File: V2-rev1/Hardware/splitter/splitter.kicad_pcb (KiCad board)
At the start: 2 copper layers, 29 parts, among them J0 Rpi_40Pin_F, J1 Control_seg:1, J2 Control_seg:2, J3 Control_seg:3, J4 Molex_PSU_F, J5 USB_A_F, J6 Siren, J7 Siren, K0 RELRAS0515, Q1 BD139-16

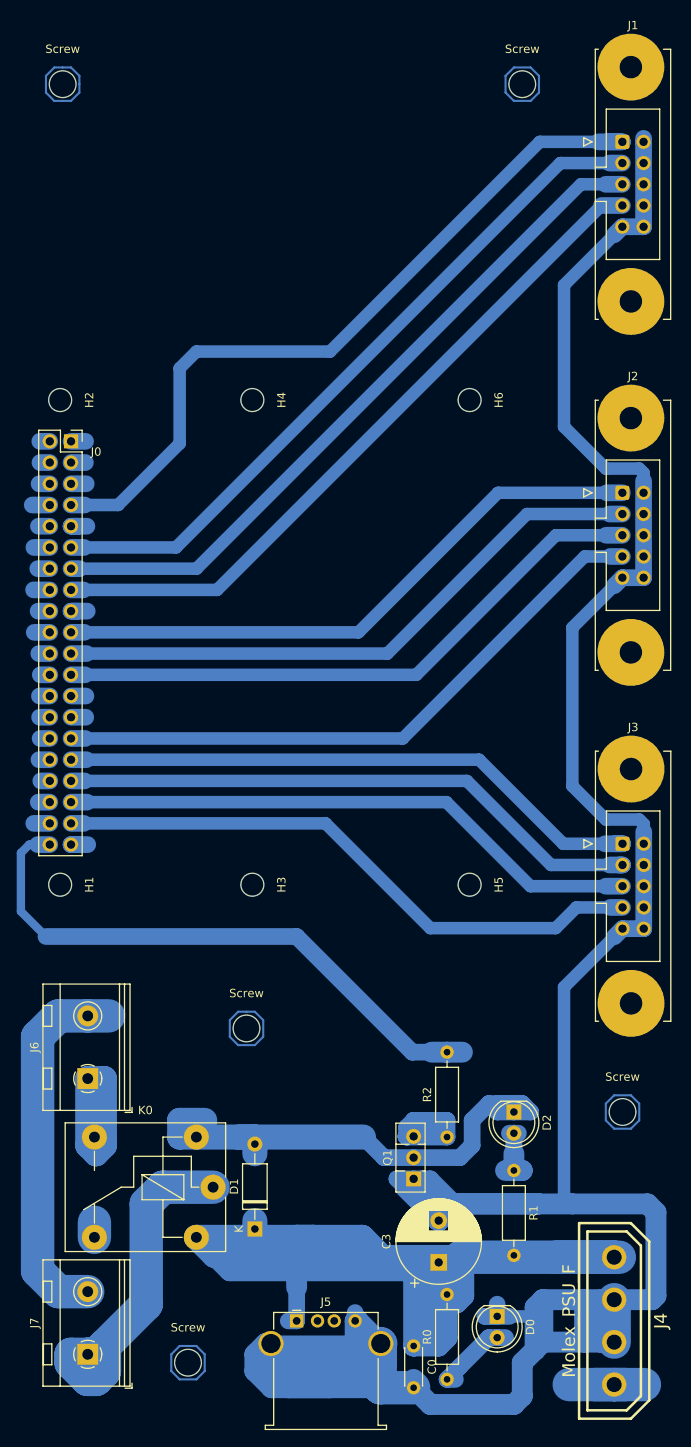
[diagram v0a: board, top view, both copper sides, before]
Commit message: make way for usb
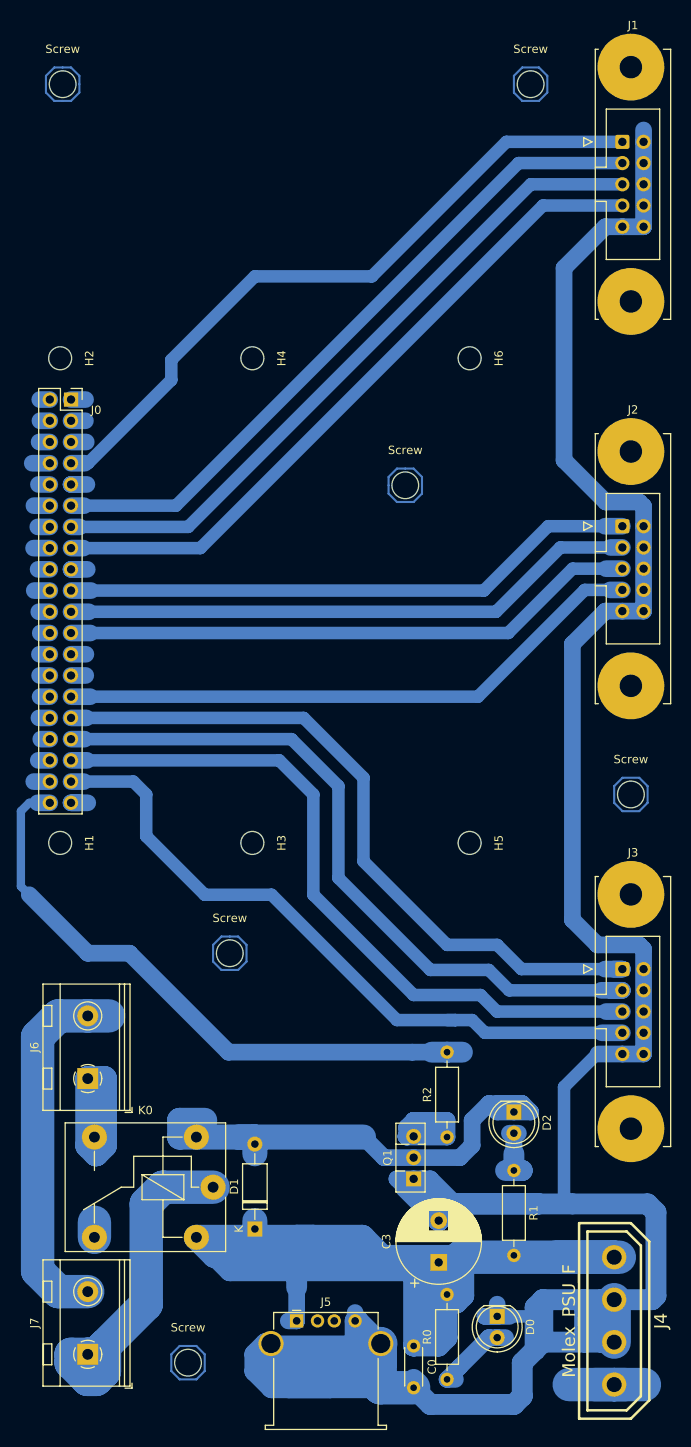
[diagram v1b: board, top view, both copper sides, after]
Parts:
- removed the Screw at (77.0, 145.0)
- removed the Screw at (122.0, 155.0)
- removed the Screw at (110.0, 32.0)
- added Screw: MountingHole_3.2mm_M3, MountingHole:MountingHole_3.2mm_M3, F.Cu at (96.0, 80.0)
- added Screw: MountingHole_3.2mm_M3, MountingHole:MountingHole_3.2mm_M3, F.Cu at (123.0, 117.0)
- added Screw: MountingHole_3.2mm_M3, MountingHole:MountingHole_3.2mm_M3, F.Cu at (75.0, 136.0)
- added Screw: MountingHole_3.2mm_M3, MountingHole:MountingHole_3.2mm_M3, F.Cu at (111.0, 32.0)
- moved J3 15.0 mm to (122.0, 137.9)
- moved H1 5.00 mm to (54.7, 122.8)
- moved H2 5.00 mm to (54.7, 64.8)
- moved H3 5.00 mm to (77.7, 122.8)
- moved H4 5.00 mm to (77.7, 64.8)
- moved H5 5.00 mm to (103.7, 122.8)
- moved H6 5.00 mm to (103.7, 64.8)
- moved J0 5.00 mm to (56.0, 69.7)
- moved J2 4.00 mm to (122.0, 84.9)
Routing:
- net /seg:3_bit:b_gpio:13: track 71.7 -> 87.4 mm
- net /seg:3_bit:c_gpio:19: track 70.2 -> 85.5 mm
- net /seg:3_bit:a_gpio:06: track 72.3 -> 86.4 mm
- net (no net): track 68.3 -> 81.9 mm, vias 11 -> 12
- net /seg:3_bit:d_gpio:26: track 72.2 -> 82.4 mm
- net /seg:1_bit:a_gpio:04: track 93.3 -> 84.5 mm
- net Earth: track 443.5 -> 438.6 mm
- net /seg:2_bit:a_gpio:10: track 72.9 -> 69.2 mm
- net /seg:2_bit:d_gpio:05: track 75.0 -> 71.3 mm
- net /seg:2_bit:c_gpio:11: track 72.9 -> 69.2 mm
- net /seg:2_bit:b_gpio:09: track 72.9 -> 69.3 mm
- net /SIREN_gpio:21: track 70.7 -> 73.9 mm
- net /seg:1_bit:d_gpio:22: track 85.0 -> 83.0 mm
- net /seg:1_bit:c_gpio:27: track 85.0 -> 83.0 mm
- net /seg:1_bit:b_gpio:17: track 85.0 -> 83.0 mm

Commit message: mark pin 1
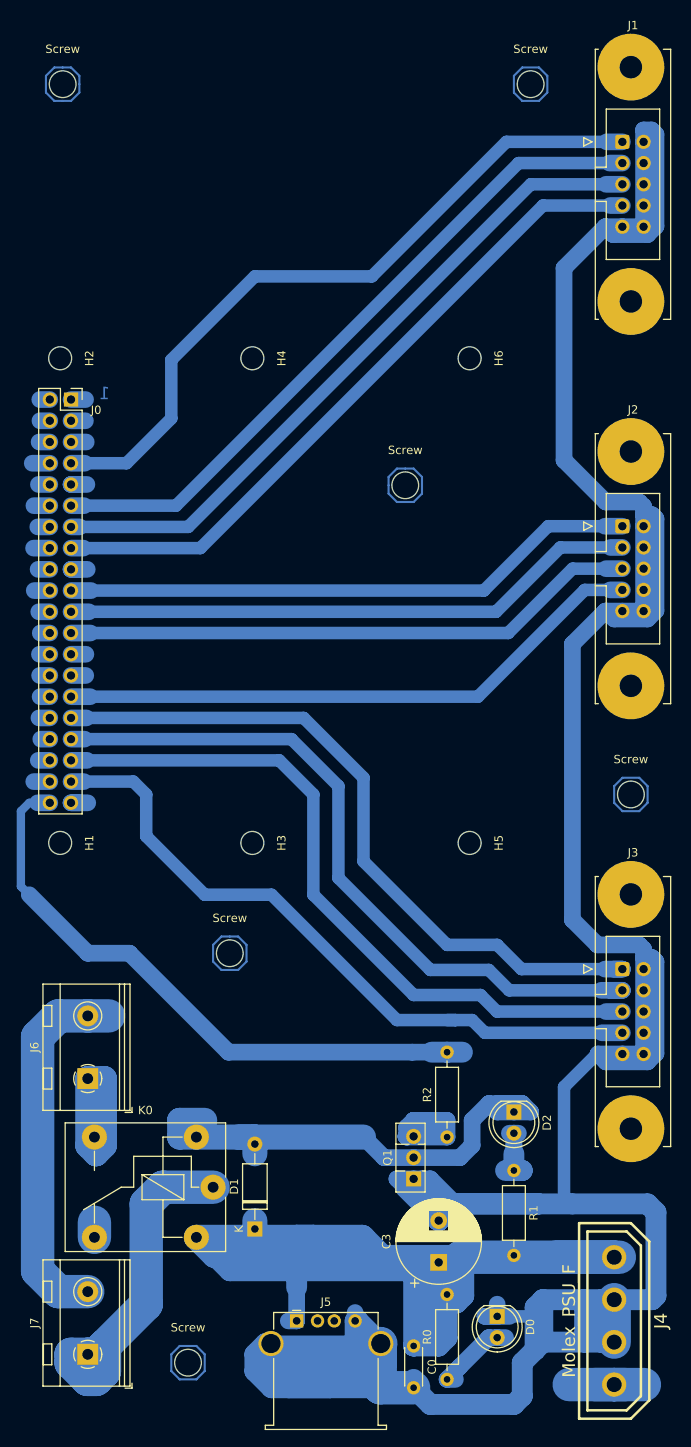
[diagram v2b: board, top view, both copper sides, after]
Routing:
- net Earth: track 438.6 -> 498.0 mm
- net /seg:1_bit:a_gpio:04: track 84.5 -> 87.6 mm
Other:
- board text added: "1"
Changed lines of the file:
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@@
   (general
     (thickness 1.6)
-    (drawings 16)
-    (tracks 461)
+    (drawings 17)
+    (tracks 487)
     (zones 0)
     (modules 30)
@@
   )
   (setup
-    (last_trace_width 1.5)
+    (last_trace_width 2)
     (user_trace_width 1)
     (user_trace_width 1.5)
@@
       (effects (font (size 1 1) (thickness 0.15)))
     )
-    (fp_text user %R (at 0.3 0) (layer F.Fab)
-      (effects (font (size 1 1) (thickness 0.15)))
-    )
     (fp_circle (center 0 0) (end 3.45 0) (layer F.CrtYd) (width 0.05))
     (fp_circle (center 0 0) (end 3.2 0) (layer Cmts.User) (width 0.15))
+    (fp_text user %R (at 0.3 0) (layer F.Fab)
+      (effects (font (size 1 1) (thickness 0.15)))
+    )
     (pad 1 np_thru_hole circle (at 0 0) (size 3.2 3.2) (drill 3.2) (layers *.Cu *.Mask))
   )
@@
       (effects (font (size 1 1) (thickness 0.15)))
     )
-    (fp_text user %R (at 0.3 0) (layer F.Fab)
-      (effects (font (size 1 1) (thickness 0.15)))
-    )
     (fp_circle (center 0 0) (end 3.45 0) (layer F.CrtYd) (width 0.05))
     (fp_circle (center 0 0) (end 3.2 0) (layer Cmts.User) (width 0.15))
+    (fp_text user %R (at 0.3 0) (layer F.Fab)
+      (effects (font (size 1 1) (thickness 0.15)))
+    )
     (pad 1 np_thru_hole circle (at 0 0) (size 3.2 3.2) (drill 3.2) (layers *.Cu *.Mask))
   )
@@
     )
     (fp_text value Control_seg:2 (at 1.27 24.1) (layer F.Fab)
-      (effects (font (size 1 1) (thickness 0.15)))
-    )
-    (fp_text user %R (at 1.27 5.08 90) (layer F.Fab)
       (effects (font (size 1 1) (thickness 0.15)))
     )
@@
     (fp_line (start -2.13 -10.97) (end 5.67 -10.97) (layer F.Fab) (width 0.1))
     (fp_line (start -3.13 -9.97) (end -2.13 -10.97) (layer F.Fab) (width 0.1))
+    (fp_text user %R (at 1.27 5.08 90) (layer F.Fab)
+      (effects (font (size 1 1) (thickness 0.15)))
+    )
     (pad 1 thru_hole roundrect (at 0 0) (size 1.7 1.7) (drill 1) (layers *.Cu *.Mask) (roundrect_rratio 0.1470588235294118)
       (net 24 /seg:2_bit:a_gpio:10))
@@
     )
   )
+  (gr_text 1 (at 60 69) (layer B.Cu)
+    (effects (font (size 1.5 1.5) (thickness 0.3)) (justify mirror))
+  )
   (gr_line (start 107.2 123.3) (end 107.2 64.3) (layer Eco2.User) (width 0.2))
   (gr_arc (start 104.2 123.3) (end 104.2 126.3) (angle -90) (layer Eco2.User) (width 0.2))
@@
   (segment (start 115 165) (end 115 152) (width 1.5) (layer B.Cu) (net 1))
   (segment (start 116 166) (end 115 165) (width 1.5) (layer B.Cu) (net 1))
-  (segment (start 124.52 137.9) (end 124.52 135.52) (width 1.5) (layer B.Cu) (net 1))
   (segment (start 124.52 148.06) (end 124.52 135.52) (width 2) (layer B.Cu) (net 1))
   (segment (start 124.52 148.06) (end 124.52 137.9) (width 1.5) (layer B.Cu) (net 1))
@@
   (segment (start 124.52 95.06) (end 124.52 84.9) (width 2) (layer B.Cu) (net 1))
   (segment (start 116 132) (end 116 99) (width 2) (layer B.Cu) (net 1))
-  (segment (start 119.94 95.06) (end 121.98 95.06) (width 2) (layer B.Cu) (net 1))
   (segment (start 116 99) (end 119.94 95.06) (width 2) (layer B.Cu) (net 1))
   (segment (start 124 135) (end 124.52 135.52) (width 2) (layer B.Cu) (net 1))
@@
   (segment (start 124.52 82.52) (end 124 82) (width 2) (layer B.Cu) (net 1))
   (segment (start 124 82) (end 120 82) (width 2) (layer B.Cu) (net 1))
-  (segment (start 124.52 84.9) (end 124.52 82.52) (width 2) (layer B.Cu) (net 1))
+  (segment (start 124.52 37.48) (end 125.48 37.48) (width 2) (layer B.Cu) (net 1))
+  (segment (start 125.48 37.48) (end 126 38) (width 2) (layer B.Cu) (net 1))
+  (segment (start 126 38) (end 126 49) (width 2) (layer B.Cu) (net 1))
+  (segment (start 126 49) (end 125 50) (width 2) (layer B.Cu) (net 1))
+  (segment (start 120.88 50) (end 119.94 49.06) (width 2) (layer B.Cu) (net 1))
+  (segment (start 125 50) (end 120.88 50) (width 2) (layer B.Cu) (net 1))
+  (segment (start 124.52 83.52) (end 125.52 83.52) (width 2) (layer B.Cu) (net 1))
+  (segment (start 124.52 84.9) (end 124.52 83.52) (width 2) (layer B.Cu) (net 1))
+  (segment (start 124.52 83.52) (end 124.52 82.52) (width 2) (layer B.Cu) (net 1))
+  (segment (start 125.52 83.52) (end 126 84) (width 2) (layer B.Cu) (net 1))
+  (segment (start 126 84) (end 126 95) (width 2) (layer B.Cu) (net 1))
+  (segment (start 126 95) (end 125 96) (width 2) (layer B.Cu) (net 1))
+  (segment (start 121 96) (end 120.06 95.06) (width 2) (layer B.Cu) (net 1))
+  (segment (start 125 96) (end 121 96) (width 2) (layer B.Cu) (net 1))
+  (segment (start 120.06 95.06) (end 121.98 95.06) (width 2) (layer B.Cu) (net 1))
+  (segment (start 119.94 95.06) (end 120.06 95.06) (width 2) (layer B.Cu) (net 1))
+  (segment (start 124.52 136.52) (end 125.52 136.52) (width 2) (layer B.Cu) (net 1))
+  (segment (start 124.52 137.9) (end 124.52 136.52) (width 1.5) (layer B.Cu) (net 1))
+  (segment (start 124.52 136.52) (end 124.52 135.52) (width 1.5) (layer B.Cu) (net 1))
+  (segment (start 125.52 136.52) (end 126 137) (width 2) (layer B.Cu) (net 1))
+  (segment (start 126 137) (end 126 148) (width 2) (layer B.Cu) (net 1))
+  (segment (start 126 148) (end 125 149) (width 2) (layer B.Cu) (net 1))
+  (segment (start 120 149) (end 119.06 148.06) (width 2) (layer B.Cu) (net 1))
+  (segment (start 125 149) (end 120 149) (width 2) (layer B.Cu) (net 1))
   (segment (start 101 187) (end 102 187) (width 2) (layer B.Cu) (net 2))
   (segment (start 102.5 185.5) (end 101 187) (width 2) (layer B.Cu) (net 2))
@@
   (segment (start 56 77.36) (end 57.202081 77.36) (width 1.5) (layer B.Cu) (net 12))
   (segment (start 56 77.36) (end 57.64 77.36) (width 2) (layer B.Cu) (net 12))
-  (segment (start 58.03773 77.36) (end 68 67.39773) (width 1.5) (layer B.Cu) (net 12))
   (segment (start 57.64 77.36) (end 58.03773 77.36) (width 1.5) (layer B.Cu) (net 12))
-  (segment (start 68 67.39773) (end 68 65) (width 1.5) (layer B.Cu) (net 12))
+  (segment (start 78 55) (end 92 55) (width 1.5) (layer B.Cu) (net 12))
+  (segment (start 92 55) (end 108.1 38.9) (width 1.5) (layer B.Cu) (net 12))
+  (segment (start 68 72) (end 68 65) (width 1.5) (layer B.Cu) (net 12))
   (segment (start 68 65) (end 78 55) (width 1.5) (layer B.Cu) (net 12))
-  (segment (start 78 55) (end 92 55) (width 1.5) (layer B.Cu) (net 12))
-  (segment (start 108.1 38.9) (end 121.98 38.9) (width 1.5) (layer B.Cu) (net 12))
-  (segment (start 92 55) (end 108.1 38.9) (width 1.5) (layer B.Cu) (net 12))
+  (segment (start 62.64 77.36) (end 68 72) (width 1.5) (layer B.Cu) (net 12))
+  (segment (start 57.64 77.36) (end 62.64 77.36) (width 1.5) (layer B.Cu) (net 12))
+  (segment (start 121.98 38.9) (end 120.1 38.9) (width 2) (layer B.Cu) (net 12))
+  (segment (start 108.1 38.9) (end 120.1 38.9) (width 1.5) (layer B.Cu) (net 12))
   (segment (start 53.46 77.36) (end 51.36 77.36) (width 2) (layer B.Cu) (net 13))
   (segment (start 56 79.9) (end 56.9 79.9) (width 2) (layer B.Cu) (net 14))
@@
   (segment (start 56 82.44) (end 57.56 82.44) (width 2) (layer B.Cu) (net 16))
   (segment (start 57.56 82.44) (end 68.56 82.44) (width 1.5) (layer B.Cu) (net 16))
-  (segment (start 109.56 41.44) (end 121.98 41.44) (width 1.5) (layer B.Cu) (net 16))
   (segment (start 68.56 82.44) (end 109.56 41.44) (width 1.5) (layer B.Cu) (net 16))
+  (segment (start 121.98 41.44) (end 120.44 41.44) (width 2) (layer B.Cu) (net 16))
+  (segment (start 109.56 41.44) (end 120.44 41.44) (width 1.5) (layer B.Cu) (net 16))
   (segment (start 53.46 82.44) (end 51.56 82.44) (width 2) (layer B.Cu) (net 17))
   (segment (start 56 84.98) (end 57.02 84.98) (width 2) (layer B.Cu) (net 18))
   (segment (start 57.02 84.98) (end 70.02 84.98) (width 1.5) (layer B.Cu) (net 18))
-  (segment (start 111.02 43.98) (end 121.98 43.98) (width 1.5) (layer B.Cu) (net 18))
   (segment (start 70.02 84.98) (end 111.02 43.98) (width 1.5) (layer B.Cu) (net 18))
+  (segment (start 121.98 43.98) (end 120.02 43.98) (width 2) (layer B.Cu) (net 18))
+  (segment (start 111.02 43.98) (end 120.02 43.98) (width 1.5) (layer B.Cu) (net 18))
   (segment (start 53.46 84.98) (end 52.02 84.98) (width 2) (layer B.Cu) (net 19))
   (segment (start 56 87.52) (end 57.48 87.52) (width 2) (layer B.Cu) (net 20))
   (segment (start 57.48 87.52) (end 71.48 87.52) (width 1.5) (layer B.Cu) (net 20))
-  (segment (start 112.48 46.52) (end 121.98 46.52) (width 1.5) (layer B.Cu) (net 20))
   (segment (start 71.48 87.52) (end 112.48 46.52) (width 1.5) (layer B.Cu) (net 20))
+  (segment (start 121.98 46.52) (end 120.52 46.52) (width 2) (layer B.Cu) (net 20))
+  (segment (start 112.48 46.52) (end 120.52 46.52) (width 1.5) (layer B.Cu) (net 20))
   (segment (start 53.46 87.52) (end 51.52 87.52) (width 2) (layer B.Cu) (net 21))
   (segment (start 56 90.06) (end 56.94 90.06) (width 2) (layer B.Cu) (net 22))

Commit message: reinforce some copper
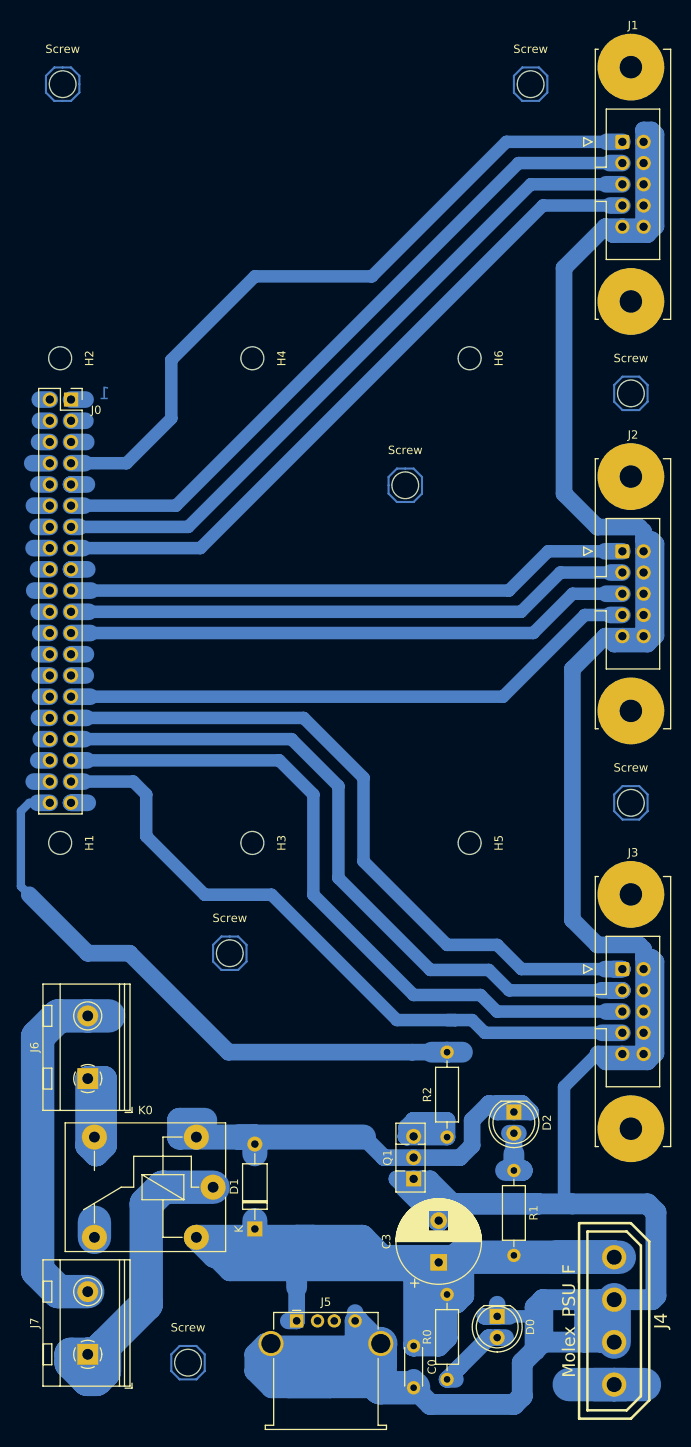
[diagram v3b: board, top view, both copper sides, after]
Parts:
- removed the Screw at (123.0, 117.0)
- added Screw: MountingHole_3.2mm_M3, MountingHole:MountingHole_3.2mm_M3, F.Cu at (123.0, 69.0)
- added Screw: MountingHole_3.2mm_M3, MountingHole:MountingHole_3.2mm_M3, F.Cu at (123.0, 118.0)
- moved J2 3.00 mm to (122.0, 87.9)
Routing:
- net (no net): track 81.9 -> 95.6 mm, vias 12 -> 13
- net /seg:2_bit:d_gpio:05: track 71.3 -> 70.0 mm
- net /seg:2_bit:c_gpio:11: track 69.2 -> 67.9 mm
- net /seg:2_bit:a_gpio:10: track 69.2 -> 67.9 mm
- net /seg:2_bit:b_gpio:09: track 69.3 -> 68.1 mm
- net Earth: track 498.0 -> 498.6 mm
